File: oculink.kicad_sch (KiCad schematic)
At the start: 46 parts, among them J2 OCuLink_x4_Amphenol_G14A42121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, J3 OCuLink_x4_Amphenol_G14A42121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, U10 ESD204DQAR, U11 ESD204DQAR, U12 ESD204DQAR, U13 ESD204DQAR, U5 ESD204DQAR, U7 ESD204DQAR, U8 ESD204DQAR, U9 ESD204DQAR

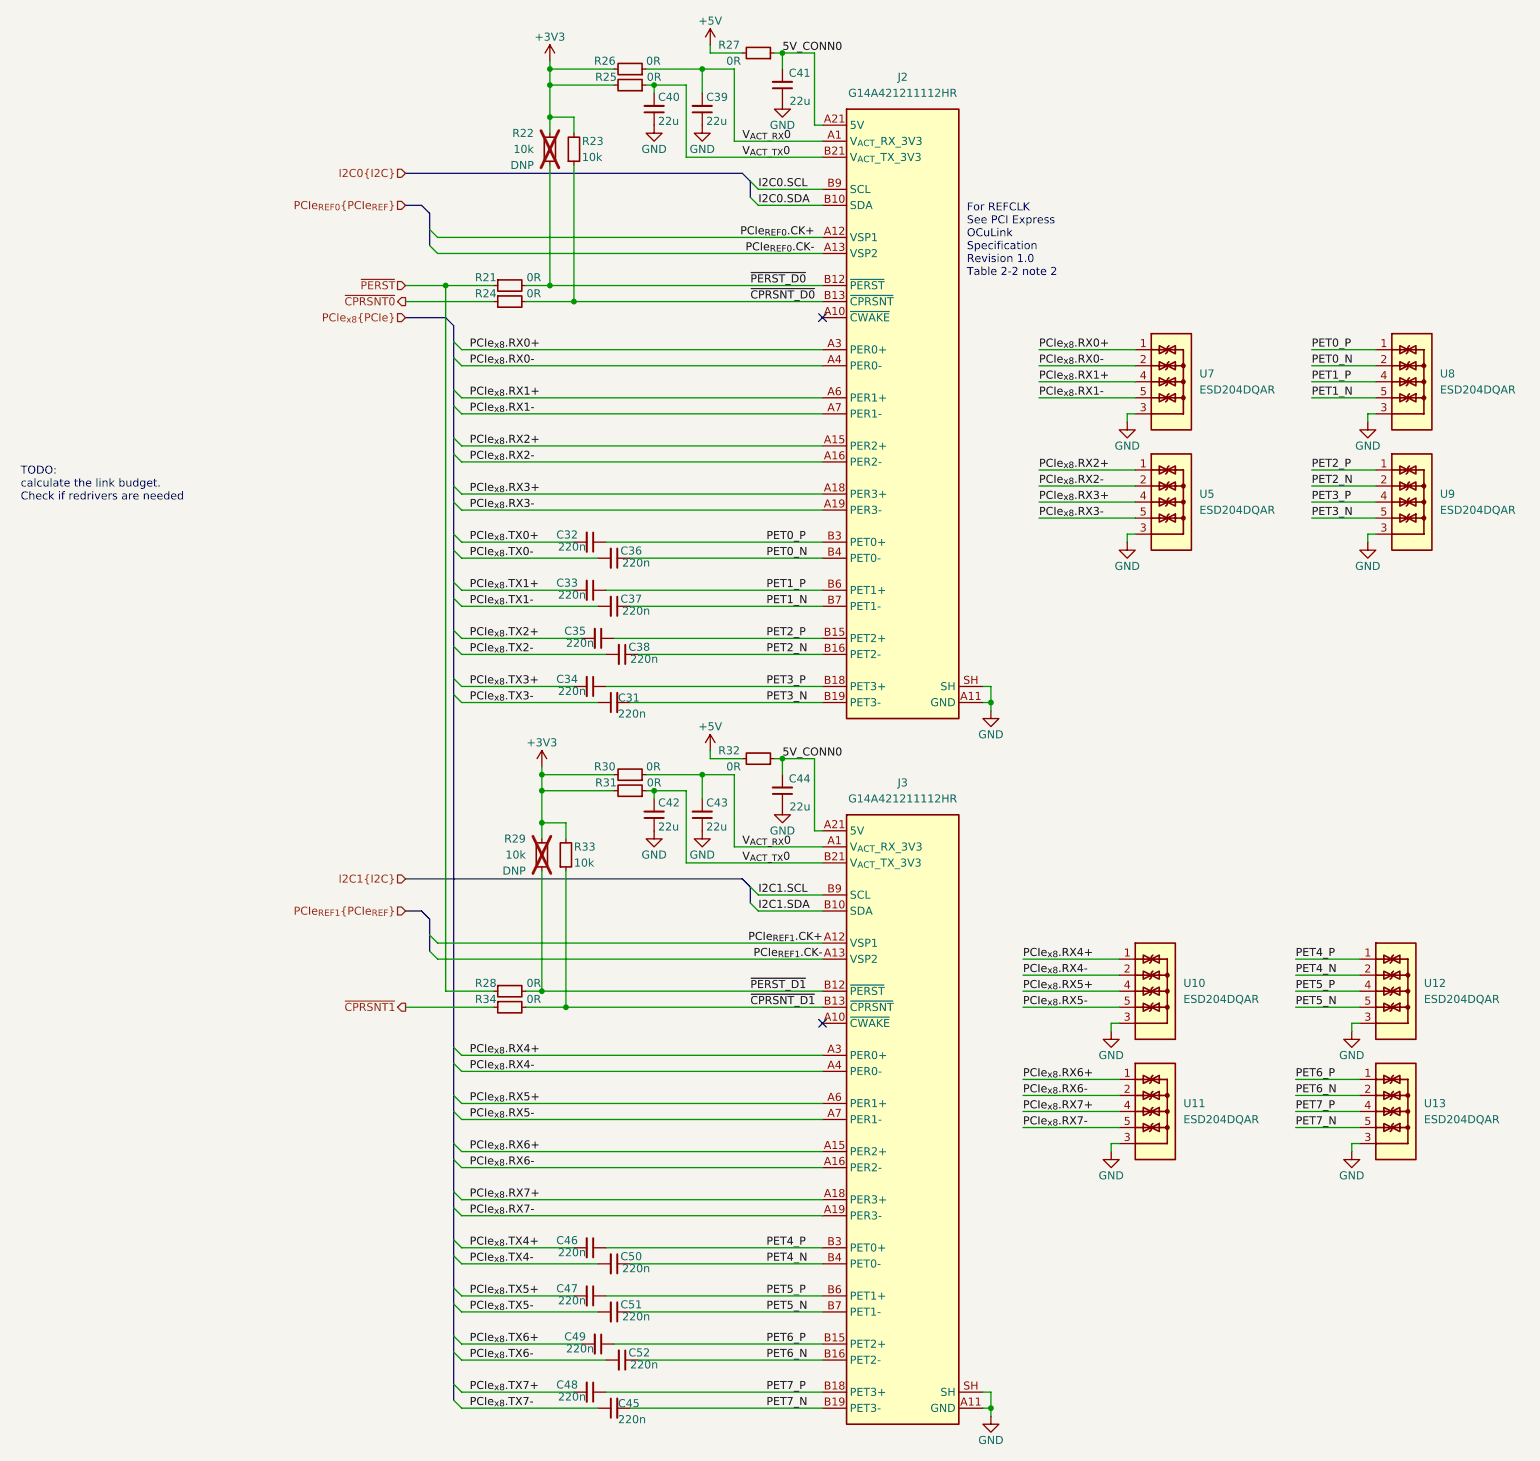
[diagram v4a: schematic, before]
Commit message: [#57056] Update PCIe lane assignment, drop 2nd OCuLink
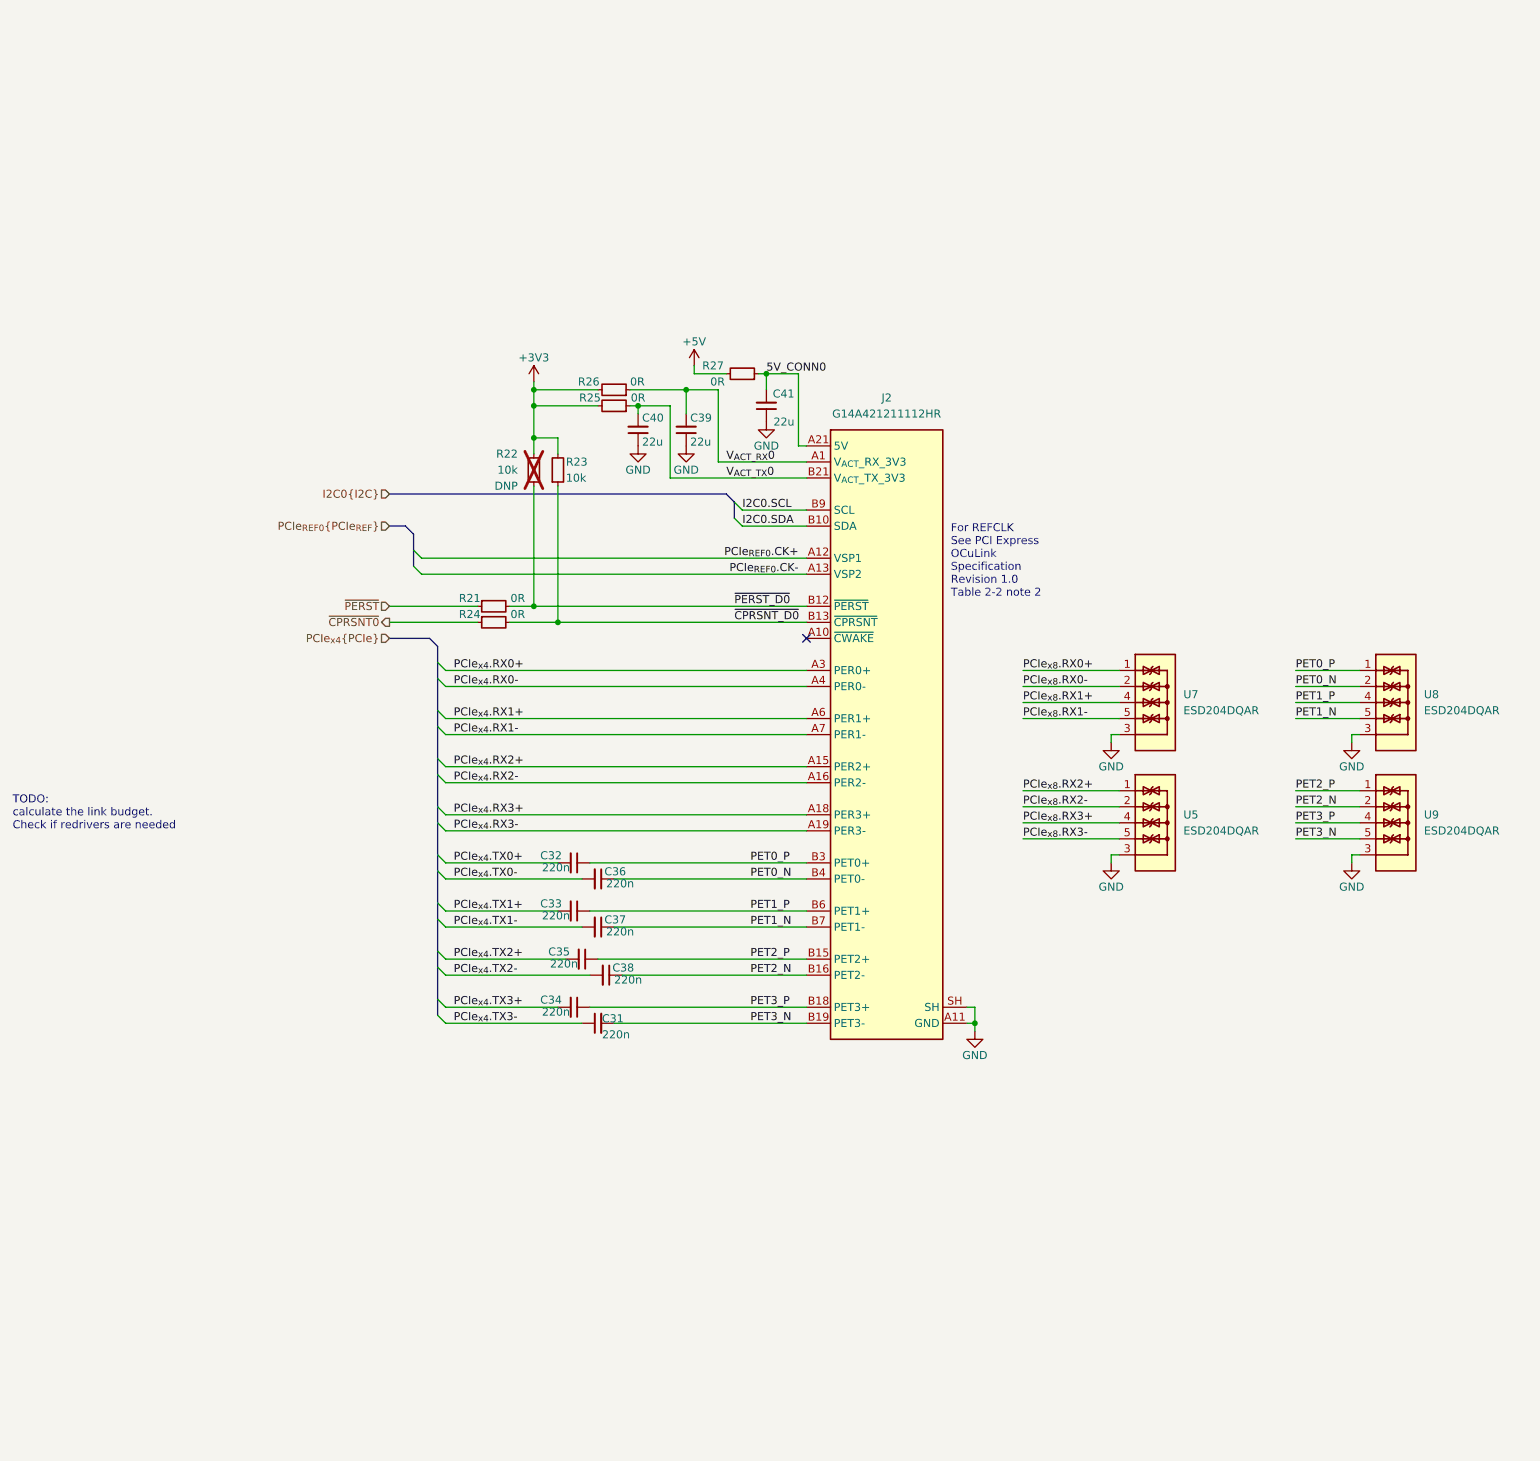
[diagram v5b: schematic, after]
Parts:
- removed C42, C43, C44: C_22u_0603, antmicro-footprints:C_0603_1608Metric, symbol antmicroCapacitors0603:C_22u_0603
- removed C45, C46, C47, C48, C49, C50, C51, C52: C_220n_0402, antmicro-footprints:C_0402_1005Metric, symbol antmicroCapacitors0402:C_220n_0402
- removed J3: OCuLink_x4_Amphenol_G14A421211112HR, antmicro-footprints:Amphenol_G14A421211112HR, symbol antmicroPciConnectors:OCuLink_x4_Amphenol_G14A421211112HR
- removed R28, R30, R31, R34: R_0R_0402, antmicro-footprints:R_0402_1005Metric, symbol antmicroResistors0402:R_0R_0402
- removed R29, R33: R_10k_0402, antmicro-footprints:R_0402_1005Metric, symbol antmicroResistors0402:R_10k_0402
- removed R32: R_0R_0603, antmicro-footprints:R_0603_1608Metric, symbol antmicroResistors0603:R_0R_0603
- removed U10, U11, U12, U13: ESD204DQAR, antmicro-footprints:USON-10_2.5x1mm_P0.5mm, symbol antmicroTVSDiodes:ESD204DQAR
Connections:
- net PCIe_{x8}.RX0+: no longer J2.A3 (PER0+)
- net PCIe_{x8}.RX0-: no longer J2.A4 (PER0-)
- net PCIe_{x8}.RX1+: no longer J2.A6 (PER1+)
- net PCIe_{x8}.RX1-: no longer J2.A7 (PER1-)
- net PCIe_{x8}.RX2+: no longer J2.A15 (PER2+)
- net PCIe_{x8}.RX2-: no longer J2.A16 (PER2-)
- net PCIe_{x8}.RX3+: no longer J2.A18 (PER3+)
- net PCIe_{x8}.RX3-: no longer J2.A19 (PER3-)
- net PCIe_{x8}.TX0+ renamed PCIe_{x4}.TX0+
- net PCIe_{x8}.TX0- renamed PCIe_{x4}.TX0-
- net PCIe_{x8}.TX1+ renamed PCIe_{x4}.TX1+
- net PCIe_{x8}.TX1- renamed PCIe_{x4}.TX1-
- net PCIe_{x8}.TX2+ renamed PCIe_{x4}.TX2+
- net PCIe_{x8}.TX2- renamed PCIe_{x4}.TX2-
- net PCIe_{x8}.TX3+ renamed PCIe_{x4}.TX3+
- net PCIe_{x8}.TX3- renamed PCIe_{x4}.TX3-
- new net PCIe_{x4}.RX0+: J2.A3 (PER0+)
- new net PCIe_{x4}.RX0-: J2.A4 (PER0-)
- new net PCIe_{x4}.RX1+: J2.A6 (PER1+)
- new net PCIe_{x4}.RX1-: J2.A7 (PER1-)
- new net PCIe_{x4}.RX2+: J2.A15 (PER2+)
- new net PCIe_{x4}.RX2-: J2.A16 (PER2-)
- new net PCIe_{x4}.RX3+: J2.A18 (PER3+)
- new net PCIe_{x4}.RX3-: J2.A19 (PER3-)
- no-connect marks 2 -> 1
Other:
- moved on the sheet: C31, C32, C33, C34, C35, C36, C37, C38, C39, C40, C41, J2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

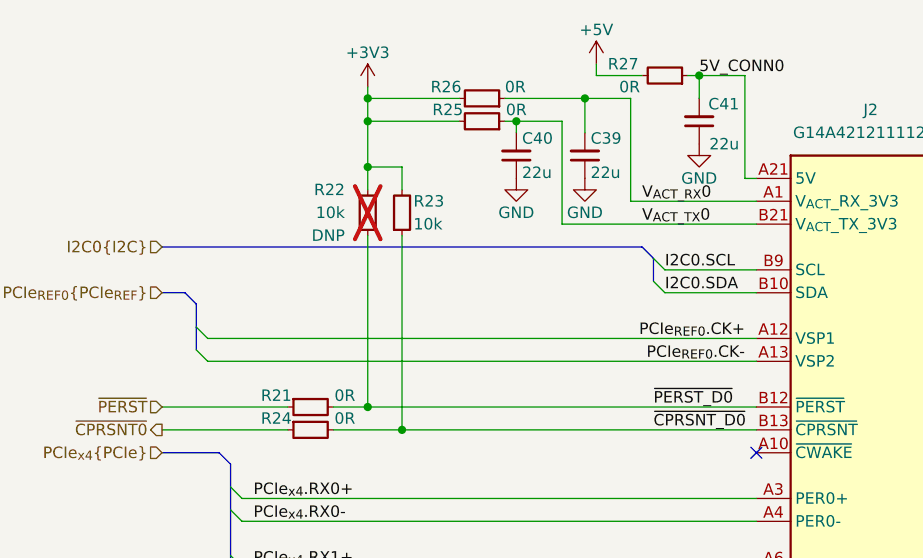
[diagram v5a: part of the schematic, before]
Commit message: [#57056] Add GPIO expander. Connect GPIOs and SMBus lines
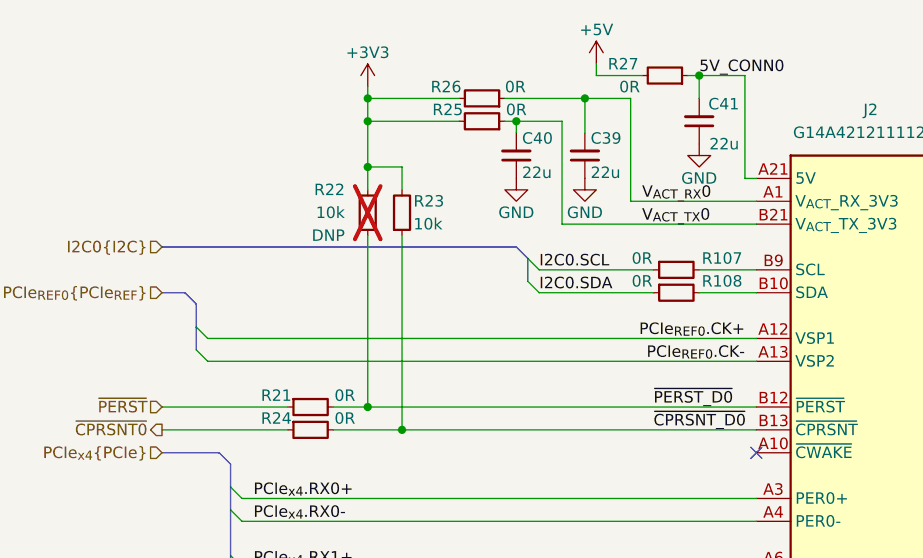
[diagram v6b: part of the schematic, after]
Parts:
- added R107, R108: R_0R_0402, antmicro-footprints:R_0402_1005Metric, symbol antmicroResistors0402:R_0R_0402
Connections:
- net I2C0.SCL: now also R107.1; no longer J2.B9 (SCL)
- net I2C0.SDA: now also R108.1; no longer J2.B10 (SDA)
- new net: J2.B10 (SDA), R108.2
- new net: J2.B9 (SCL), R107.2
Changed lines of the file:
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@@
     (company "Antmicro Ltd.")
   )
-  (bus_alias "I2C" (members "SDA" "SCL"))
+  (bus_alias "I2C" (members "SDA" "SCL" "~{INT}"))
   (junction (at 210.82 92.71) (diameter 0) (color 0 0 0 0)
   )
@@
   )
   (no_connect (at 237.49 129.54))
-  (bus_entry (at 227.33 109.22) (size -1.27 -1.27)
+  (bus_entry (at 213.36 109.22) (size -1.27 -1.27)
     (stroke (width 0) (type default))
   )
@@
     (stroke (width 0) (type default))
   )
-  (bus_entry (at 227.33 111.76) (size -1.27 -1.27)
+  (bus_entry (at 213.36 111.76) (size -1.27 -1.27)
     (stroke (width 0) (type default))
   )
@@
     (stroke (width 0) (type default))
   )
+  (wire (pts (xy 231.14 111.76) (xy 237.49 111.76))
+    (stroke (width 0) (type default))
+  )
   (wire (pts (xy 198.12 97.79) (xy 194.31 97.79))
     (stroke (width 0) (type default))
@@
     (stroke (width 0) (type default))
   )
-  (bus (pts (xy 226.06 107.95) (xy 226.06 110.49))
+  (bus (pts (xy 212.09 107.95) (xy 212.09 110.49))
     (stroke (width 0) (type default))
   )
@@
     (stroke (width 0) (type default))
   )
-  (wire (pts (xy 227.33 109.22) (xy 237.49 109.22))
-    (stroke (width 0) (type default))
-  )
   (wire (pts (xy 237.49 152.4) (xy 180.34 152.4))
     (stroke (width 0) (type default))
@@
     (stroke (width 0) (type default))
   )
-  (bus (pts (xy 171.45 106.68) (xy 224.79 106.68))
+  (bus (pts (xy 171.45 106.68) (xy 210.82 106.68))
     (stroke (width 0) (type default))
   )
@@
     (stroke (width 0) (type default))
   )
+  (wire (pts (xy 213.36 109.22) (xy 226.06 109.22))
+    (stroke (width 0) (type default))
+  )
   (bus (pts (xy 173.99 111.76) (xy 171.45 111.76))
     (stroke (width 0) (type default))
@@
     (stroke (width 0) (type default))
   )
+  (wire (pts (xy 231.14 109.22) (xy 237.49 109.22))
+    (stroke (width 0) (type default))
+  )
   (wire (pts (xy 323.85 165.1) (xy 323.85 163.83))
     (stroke (width 0) (type default))
@@
     (stroke (width 0) (type default))
   )
-  (bus (pts (xy 226.06 107.95) (xy 224.79 106.68))
+  (wire (pts (xy 213.36 111.76) (xy 226.06 111.76))
+    (stroke (width 0) (type default))
+  )
+  (bus (pts (xy 212.09 107.95) (xy 210.82 106.68))
     (stroke (width 0) (type default))
   )
@@
   )
   (wire (pts (xy 314.96 139.7) (xy 325.12 139.7))
-    (stroke (width 0) (type default))
-  )
-  (wire (pts (xy 227.33 111.76) (xy 237.49 111.76))
     (stroke (width 0) (type default))
   )
@@
     (effects (font (size 1.27 1.27)) (justify left bottom))
   )
-  (label "I2C0.SDA" (at 227.33 111.76 0) (fields_autoplaced)
+  (label "I2C0.SDA" (at 213.36 111.76 0) (fields_autoplaced)
     (effects (font (size 1.27 1.27)) (justify left bottom))
   )
@@
     (effects (font (size 1.27 1.27)) (justify left bottom))
   )
-  (label "I2C0.SCL" (at 227.33 109.22 0) (fields_autoplaced)
+  (label "I2C0.SCL" (at 213.36 109.22 0) (fields_autoplaced)
     (effects (font (size 1.27 1.27)) (justify left bottom))
   )
@@
     )
   )
+  (symbol (lib_id "antmicroResistors0402:R_0R_0402") (at 226.06 109.22 0) (unit 1)
+    (in_bom yes) (on_board yes) (dnp no)
+    (property "Reference" "R107" (at 233.68 107.95 0)
+      (effects (font (size 1.27 1.27) (thickness 0.15)))
+    )
+    (property "Value" "R_0R_0402" (at 246.38 121.92 0)
+      (effects (font (size 1.27 1.27) (thickness 0.15)) (justify left bottom) hide)
+    )
+    (property "Footprint" "antmicro-footprints:R_0402_1005Metric" (at 246.38 124.46 0)
+      (effects (font (size 1.27 1.27) (thickness 0.15)) (justify left bottom) hide)
+    )
+    (property "Datasheet" "https://industrial.panasonic.com/cdbs/www-data/pdf/RDA0000/AOA0000C301.pdf" (at 246.38 127 0)
+      (effects (font (size 1.27 1.27) (thickness 0.15)) (justify left bottom) hide)
+    )
+    (property "MPN" "ERJ2GE0R00X" (at 246.38 129.54 0)
+      (effects (font (size 1.27 1.27) (thickness 0.15)) (justify left bottom) hide)
+    )
+    (property "Manufacturer" "Panasonic" (at 246.38 132.08 0)
+      (effects (font (size 1.27 1.27) (thickness 0.15)) (justify left bottom) hide)
+    )
+    (property "License" "Apache-2.0" (at 246.38 134.62 0)
+      (effects (font (size 1.27 1.27) (thickness 0.15)) (justify left bottom) hide)
+    )
+    (property "Author" "Antmicro" (at 246.38 137.16 0)
+      (effects (font (size 1.27 1.27) (thickness 0.15)) (justify left bottom) hide)
+    )
+    (property "Val" "0R" (at 224.79 107.95 0)
+      (effects (font (size 1.27 1.27) (thickness 0.15)))
+    )
+    (property "Tolerance" "~" (at 246.38 119.38 0)
+      (effects (font (size 1.27 1.27)) (justify left bottom) hide)
+    )
+    (property "Current" "1A" (at 246.38 139.7 0)
+      (effects (font (size 1.27 1.27) (thickness 0.15)) (justify left bottom) hide)
+    )
+    (pin "2")
+    (pin "1")
+    (instances
+      (project "com-express-7-baseboard"
+        (path "/1b8c34da-dad5-4b0b-8c4b-45db766c4dfa/b09f3a23-0194-4388-b358-3a9807b09321"
+          (reference "R107") (unit 1)
+        )
+      )
+    )
+  )
   (symbol (lib_id "antmicroResistors0402:R_10k_0402") (at 198.12 105.41 90) (unit 1)
     (in_bom yes) (on_board yes) (dnp no)
@@
         )
       )
+    )
+  )
+  (symbol (lib_id "antmicroResistors0402:R_0R_0402") (at 226.06 111.76 0) (unit 1)
+    (in_bom yes) (on_board yes) (dnp no)
+    (property "Reference" "R108" (at 233.68 110.49 0)
+      (effects (font (size 1.27 1.27) (thickness 0.15)))
+    )
+    (property "Value" "R_0R_0402" (at 246.38 124.46 0)
+      (effects (font (size 1.27 1.27) (thickness 0.15)) (justify left bottom) hide)
+    )
+    (property "Footprint" "antmicro-footprints:R_0402_1005Metric" (at 246.38 127 0)
+      (effects (font (size 1.27 1.27) (thickness 0.15)) (justify left bottom) hide)
+    )
+    (property "Datasheet" "https://industrial.panasonic.com/cdbs/www-data/pdf/RDA0000/AOA0000C301.pdf" (at 246.38 129.54 0)
+      (effects (font (size 1.27 1.27) (thickness 0.15)) (justify left bottom) hide)
+    )
+    (property "MPN" "ERJ2GE0R00X" (at 246.38 132.08 0)
+      (effects (font (size 1.27 1.27) (thickness 0.15)) (justify left bottom) hide)
+    )
+    (property "Manufacturer" "Panasonic" (at 246.38 134.62 0)
+      (effects (font (size 1.27 1.27) (thickness 0.15)) (justify left bottom) hide)
+    )
+    (property "License" "Apache-2.0" (at 246.38 137.16 0)
+      (effects (font (size 1.27 1.27) (thickness 0.15)) (justify left bottom) hide)
+    )
+    (property "Author" "Antmicro" (at 246.38 139.7 0)
+      (effects (font (size 1.27 1.27) (thickness 0.15)) (justify left bottom) hide)
+    )
+    (property "Val" "0R" (at 224.79 110.49 0)
+      (effects (font (size 1.27 1.27) (thickness 0.15)))
+    )
+    (property "Tolerance" "~" (at 246.38 121.92 0)
+      (effects (font (size 1.27 1.27)) (justify left bottom) hide)
+    )
+    (property "Current" "1A" (at 246.38 142.24 0)
+      (effects (font (size 1.27 1.27) (thickness 0.15)) (justify left bottom) hide)
+    )
+    (pin "2")
+    (pin "1")
+    (instances
+      (project "com-express-7-baseboard"
+        (path "/1b8c34da-dad5-4b0b-8c4b-45db766c4dfa/b09f3a23-0194-4388-b358-3a9807b09321"
+          (reference "R108") (unit 1)
+        )
+      )
